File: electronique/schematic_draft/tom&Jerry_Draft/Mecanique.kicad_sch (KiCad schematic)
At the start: 4 parts

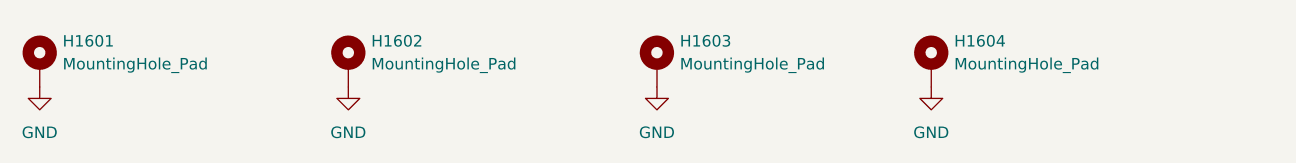
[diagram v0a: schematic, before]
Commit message: STM32 KiCAD v2.0 x CubeIDE - Pin definitif + schematic reviewed
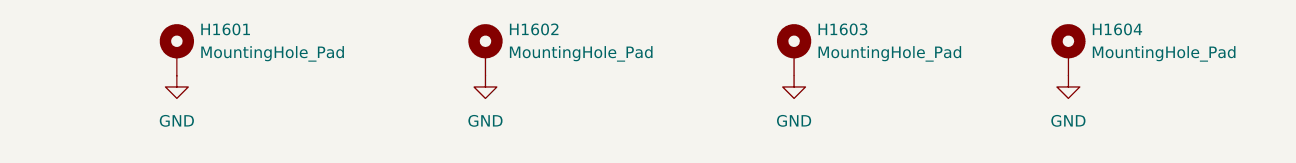
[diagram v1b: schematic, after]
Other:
- moved on the sheet: H1601, H1602, H1603, H1604
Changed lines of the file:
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@@
 	(symbol
 		(lib_id "power:GND")
-		(at 66.04 85.09 0)
+		(at 81.28 83.82 0)
 		(unit 1)
 		(exclude_from_sim no)
@@
 		(fields_autoplaced yes)
 		(property "Reference" "#PWR01601"
-			(at 66.04 91.44 0)
+			(at 81.28 90.17 0)
 			(effects
 				(font
@@
 		)
 		(property "Value" "GND"
-			(at 66.04 90.17 0)
-			(effects
-				(font
-					(size 1.27 1.27)
-				)
-			)
-		)
-		(property "Footprint" ""
-			(at 66.04 85.09 0)
+			(at 81.28 88.9 0)
+			(effects
+				(font
+					(size 1.27 1.27)
+				)
+			)
+		)
+		(property "Footprint" ""
+			(at 81.28 83.82 0)
 			(effects
 				(font
@@
 		)
 		(property "Datasheet" ""
-			(at 66.04 85.09 0)
+			(at 81.28 83.82 0)
 			(effects
 				(font
@@
 		)
 		(property "Description" "Power symbol creates a global label with name \"GND\" , ground"
-			(at 66.04 85.09 0)
+			(at 81.28 83.82 0)
 			(effects
 				(font
@@
 	(symbol
 		(lib_id "power:GND")
-		(at 165.1 85.09 0)
+		(at 180.34 83.82 0)
 		(unit 1)
 		(exclude_from_sim no)
@@
 		(fields_autoplaced yes)
 		(property "Reference" "#PWR01604"
-			(at 165.1 91.44 0)
+			(at 180.34 90.17 0)
 			(effects
 				(font
@@
 		)
 		(property "Value" "GND"
-			(at 165.1 90.17 0)
-			(effects
-				(font
-					(size 1.27 1.27)
-				)
-			)
-		)
-		(property "Footprint" ""
-			(at 165.1 85.09 0)
+			(at 180.34 88.9 0)
+			(effects
+				(font
+					(size 1.27 1.27)
+				)
+			)
+		)
+		(property "Footprint" ""
+			(at 180.34 83.82 0)
 			(effects
 				(font
@@
 		)
 		(property "Datasheet" ""
-			(at 165.1 85.09 0)
+			(at 180.34 83.82 0)
 			(effects
 				(font
@@
 		)
 		(property "Description" "Power symbol creates a global label with name \"GND\" , ground"
-			(at 165.1 85.09 0)
+			(at 180.34 83.82 0)
 			(effects
 				(font
@@
 	(symbol
 		(lib_id "Mechanical:MountingHole_Pad")
-		(at 134.62 82.55 0)
+		(at 149.86 81.28 0)
 		(unit 1)
 		(exclude_from_sim yes)
@@
 		(fields_autoplaced yes)
 		(property "Reference" "H1603"
-			(at 137.16 80.0099 0)
+			(at 152.4 78.7399 0)
 			(effects
 				(font
@@
 		)
 		(property "Value" "MountingHole_Pad"
-			(at 137.16 82.5499 0)
-			(effects
-				(font
-					(size 1.27 1.27)
-				)
-				(justify left)
-			)
-		)
-		(property "Footprint" ""
-			(at 134.62 82.55 0)
+			(at 152.4 81.2799 0)
+			(effects
+				(font
+					(size 1.27 1.27)
+				)
+				(justify left)
+			)
+		)
+		(property "Footprint" ""
+			(at 149.86 81.28 0)
 			(effects
 				(font
@@
 		)
 		(property "Datasheet" "~"
-			(at 134.62 82.55 0)
+			(at 149.86 81.28 0)
 			(effects
 				(font
@@
 		)
 		(property "Description" "Mounting Hole with connection"
-			(at 134.62 82.55 0)
+			(at 149.86 81.28 0)
 			(effects
 				(font
@@
 	(symbol
 		(lib_id "power:GND")
-		(at 100.33 85.09 0)
+		(at 115.57 83.82 0)
 		(unit 1)
 		(exclude_from_sim no)
@@
 		(fields_autoplaced yes)
 		(property "Reference" "#PWR01602"
-			(at 100.33 91.44 0)
+			(at 115.57 90.17 0)
 			(effects
 				(font
@@
 		)
 		(property "Value" "GND"
-			(at 100.33 90.17 0)
-			(effects
-				(font
-					(size 1.27 1.27)
-				)
-			)
-		)
-		(property "Footprint" ""
-			(at 100.33 85.09 0)
+			(at 115.57 88.9 0)
+			(effects
+				(font
+					(size 1.27 1.27)
+				)
+			)
+		)
+		(property "Footprint" ""
+			(at 115.57 83.82 0)
 			(effects
 				(font
@@
 		)
 		(property "Datasheet" ""
-			(at 100.33 85.09 0)
+			(at 115.57 83.82 0)
 			(effects
 				(font
@@
 		)
 		(property "Description" "Power symbol creates a global label with name \"GND\" , ground"
-			(at 100.33 85.09 0)
+			(at 115.57 83.82 0)
 			(effects
 				(font
@@
 	(symbol
 		(lib_id "power:GND")
-		(at 134.62 85.09 0)
+		(at 149.86 83.82 0)
 		(unit 1)
 		(exclude_from_sim no)
@@
 		(fields_autoplaced yes)
 		(property "Reference" "#PWR01603"
-			(at 134.62 91.44 0)
+			(at 149.86 90.17 0)
 			(effects
 				(font
@@
 		)
 		(property "Value" "GND"
-			(at 134.62 90.17 0)
-			(effects
-				(font
-					(size 1.27 1.27)
-				)
-			)
-		)
-		(property "Footprint" ""
-			(at 134.62 85.09 0)
+			(at 149.86 88.9 0)
+			(effects
+				(font
+					(size 1.27 1.27)
+				)
+			)
+		)
+		(property "Footprint" ""
+			(at 149.86 83.82 0)
 			(effects
 				(font
@@
 		)
 		(property "Datasheet" ""
-			(at 134.62 85.09 0)
+			(at 149.86 83.82 0)
 			(effects
 				(font
@@
 		)
 		(property "Description" "Power symbol creates a global label with name \"GND\" , ground"
-			(at 134.62 85.09 0)
+			(at 149.86 83.82 0)
 			(effects
 				(font
@@
 	(symbol
 		(lib_id "Mechanical:MountingHole_Pad")
-		(at 66.04 82.55 0)
+		(at 81.28 81.28 0)
 		(unit 1)
 		(exclude_from_sim yes)
@@
 		(fields_autoplaced yes)
 		(property "Reference" "H1601"
-			(at 68.58 80.0099 0)
+			(at 83.82 78.7399 0)
 			(effects
 				(font
@@
 		)
 		(property "Value" "MountingHole_Pad"
-			(at 68.58 82.5499 0)
-			(effects
-				(font
-					(size 1.27 1.27)
-				)
-				(justify left)
-			)
-		)
-		(property "Footprint" ""
-			(at 66.04 82.55 0)
+			(at 83.82 81.2799 0)
+			(effects
+				(font
+					(size 1.27 1.27)
+				)
+				(justify left)
+			)
+		)
+		(property "Footprint" ""
+			(at 81.28 81.28 0)
 			(effects
 				(font
@@
 		)
 		(property "Datasheet" "~"
-			(at 66.04 82.55 0)
+			(at 81.28 81.28 0)
 			(effects
 				(font
@@
 		)
 		(property "Description" "Mounting Hole with connection"
-			(at 66.04 82.55 0)
+			(at 81.28 81.28 0)
 			(effects
 				(font
@@
 	(symbol
 		(lib_id "Mechanical:MountingHole_Pad")
-		(at 165.1 82.55 0)
+		(at 180.34 81.28 0)
 		(unit 1)
 		(exclude_from_sim yes)
@@
 		(fields_autoplaced yes)
 		(property "Reference" "H1604"
-			(at 167.64 80.0099 0)
+			(at 182.88 78.7399 0)
 			(effects
 				(font
@@
 		)
 		(property "Value" "MountingHole_Pad"
-			(at 167.64 82.5499 0)
-			(effects
-				(font
-					(size 1.27 1.27)
-				)
-				(justify left)
-			)
-		)
-		(property "Footprint" ""
-			(at 165.1 82.55 0)
+			(at 182.88 81.2799 0)
+			(effects
+				(font
+					(size 1.27 1.27)
+				)
+				(justify left)
+			)
+		)
+		(property "Footprint" ""
+			(at 180.34 81.28 0)
 			(effects
 				(font
@@
 		)
 		(property "Datasheet" "~"
-			(at 165.1 82.55 0)
+			(at 180.34 81.28 0)
 			(effects
 				(font
@@
 		)
 		(property "Description" "Mounting Hole with connection"
-			(at 165.1 82.55 0)
+			(at 180.34 81.28 0)
 			(effects
 				(font
@@
 	(symbol
 		(lib_id "Mechanical:MountingHole_Pad")
-		(at 100.33 82.55 0)
+		(at 115.57 81.28 0)
 		(unit 1)
 		(exclude_from_sim yes)
@@
 		(fields_autoplaced yes)
 		(property "Reference" "H1602"
-			(at 102.87 80.0099 0)
+			(at 118.11 78.7399 0)
 			(effects
 				(font
@@
 		)
 		(property "Value" "MountingHole_Pad"
-			(at 102.87 82.5499 0)
-			(effects
-				(font
-					(size 1.27 1.27)
-				)
-				(justify left)
-			)
-		)
-		(property "Footprint" ""
-			(at 100.33 82.55 0)
+			(at 118.11 81.2799 0)
+			(effects
+				(font
+					(size 1.27 1.27)
+				)
+				(justify left)
+			)
+		)
+		(property "Footprint" ""
+			(at 115.57 81.28 0)
 			(effects
 				(font
@@
 		)
 		(property "Datasheet" "~"
-			(at 100.33 82.55 0)
+			(at 115.57 81.28 0)
 			(effects
 				(font
@@
 		)
 		(property "Description" "Mounting Hole with connection"
-			(at 100.33 82.55 0)
-			(effects
-				(font
+			(at 115.57 81.28 0)
+			(effects
+				(font

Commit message: Adding footprint V0.1
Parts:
- H1601, H1602, H1603, H1604: footprint (none) -> MountingHole:MountingHole_3.2mm_M3_Pad_Via
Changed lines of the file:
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@@
 			)
 		)
-		(property "Footprint" ""
+		(property "Footprint" "MountingHole:MountingHole_3.2mm_M3_Pad_Via"
 			(at 149.86 81.28 0)
 			(effects
@@
 			)
 		)
-		(property "Footprint" ""
+		(property "Footprint" "MountingHole:MountingHole_3.2mm_M3_Pad_Via"
 			(at 81.28 81.28 0)
 			(effects
@@
 			)
 		)
-		(property "Footprint" ""
+		(property "Footprint" "MountingHole:MountingHole_3.2mm_M3_Pad_Via"
 			(at 180.34 81.28 0)
 			(effects
@@
 			)
 		)
-		(property "Footprint" ""
+		(property "Footprint" "MountingHole:MountingHole_3.2mm_M3_Pad_Via"
 			(at 115.57 81.28 0)
 			(effects

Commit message: Ajout V2 TOF + MultiPCB Panalize
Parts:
- renumbered H1601 to H1101, H1602 to H1102, H1603 to H1103, H1604 to H1104
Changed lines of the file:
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@@
 		(dnp no)
 		(fields_autoplaced yes)
-		(property "Reference" "#PWR01601"
+		(property "Reference" "#PWR01101"
 			(at 81.28 90.17 0)
 			(effects
@@
 			(project ""
 				(path "/d6e3fbeb-d028-494d-83bf-2e4a8b12578d/ea2dc0aa-c072-4ac8-b7d3-16b9d53a67a9"
-					(reference "#PWR01601")
+					(reference "#PWR01101")
 					(unit 1)
 				)
@@
 		(dnp no)
 		(fields_autoplaced yes)
-		(property "Reference" "#PWR01604"
+		(property "Reference" "#PWR01104"
 			(at 180.34 90.17 0)
 			(effects
@@
 			(project "tom&Jerry_Draft"
 				(path "/d6e3fbeb-d028-494d-83bf-2e4a8b12578d/ea2dc0aa-c072-4ac8-b7d3-16b9d53a67a9"
-					(reference "#PWR01604")
+					(reference "#PWR01104")
 					(unit 1)
 				)
@@
 		(dnp no)
 		(fields_autoplaced yes)
-		(property "Reference" "H1603"
+		(property "Reference" "H1103"
 			(at 152.4 78.7399 0)
 			(effects
@@
 			(project "tom&Jerry_Draft"
 				(path "/d6e3fbeb-d028-494d-83bf-2e4a8b12578d/ea2dc0aa-c072-4ac8-b7d3-16b9d53a67a9"
-					(reference "H1603")
+					(reference "H1103")
 					(unit 1)
 				)
@@
 		(dnp no)
 		(fields_autoplaced yes)
-		(property "Reference" "#PWR01602"
+		(property "Reference" "#PWR01102"
 			(at 115.57 90.17 0)
 			(effects
@@
 			(project "tom&Jerry_Draft"
 				(path "/d6e3fbeb-d028-494d-83bf-2e4a8b12578d/ea2dc0aa-c072-4ac8-b7d3-16b9d53a67a9"
-					(reference "#PWR01602")
+					(reference "#PWR01102")
 					(unit 1)
 				)
@@
 		(dnp no)
 		(fields_autoplaced yes)
-		(property "Reference" "#PWR01603"
+		(property "Reference" "#PWR01103"
 			(at 149.86 90.17 0)
 			(effects
@@
 			(project "tom&Jerry_Draft"
 				(path "/d6e3fbeb-d028-494d-83bf-2e4a8b12578d/ea2dc0aa-c072-4ac8-b7d3-16b9d53a67a9"
-					(reference "#PWR01603")
+					(reference "#PWR01103")
 					(unit 1)
 				)
@@
 		(dnp no)
 		(fields_autoplaced yes)
-		(property "Reference" "H1601"
+		(property "Reference" "H1101"
 			(at 83.82 78.7399 0)
 			(effects
@@
 			(project ""
 				(path "/d6e3fbeb-d028-494d-83bf-2e4a8b12578d/ea2dc0aa-c072-4ac8-b7d3-16b9d53a67a9"
-					(reference "H1601")
+					(reference "H1101")
 					(unit 1)
 				)
@@
 		(dnp no)
 		(fields_autoplaced yes)
-		(property "Reference" "H1604"
+		(property "Reference" "H1104"
 			(at 182.88 78.7399 0)
 			(effects
@@
 			(project "tom&Jerry_Draft"
 				(path "/d6e3fbeb-d028-494d-83bf-2e4a8b12578d/ea2dc0aa-c072-4ac8-b7d3-16b9d53a67a9"
-					(reference "H1604")
+					(reference "H1104")
 					(unit 1)
 				)
@@
 		(dnp no)
 		(fields_autoplaced yes)
-		(property "Reference" "H1602"
+		(property "Reference" "H1102"
 			(at 118.11 78.7399 0)
 			(effects
@@
 			(project "tom&Jerry_Draft"
 				(path "/d6e3fbeb-d028-494d-83bf-2e4a8b12578d/ea2dc0aa-c072-4ac8-b7d3-16b9d53a67a9"
-					(reference "H1602")
-					(unit 1)
-				)
+					(reference "H1102")
+					(unit 1)
+				)

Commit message: Routage Signal Complet - PCB V2.0
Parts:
- renumbered H1101 to H1201, H1102 to H1202, H1103 to H1203, H1104 to H1204
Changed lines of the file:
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@@
 		(dnp no)
 		(fields_autoplaced yes)
-		(property "Reference" "#PWR01101"
+		(property "Reference" "#PWR01201"
 			(at 81.28 90.17 0)
 			(effects
@@
 			(project ""
 				(path "/d6e3fbeb-d028-494d-83bf-2e4a8b12578d/ea2dc0aa-c072-4ac8-b7d3-16b9d53a67a9"
-					(reference "#PWR01101")
+					(reference "#PWR01201")
 					(unit 1)
 				)
@@
 		(dnp no)
 		(fields_autoplaced yes)
-		(property "Reference" "#PWR01104"
+		(property "Reference" "#PWR01204"
 			(at 180.34 90.17 0)
 			(effects
@@
 			(project "tom&Jerry_Draft"
 				(path "/d6e3fbeb-d028-494d-83bf-2e4a8b12578d/ea2dc0aa-c072-4ac8-b7d3-16b9d53a67a9"
-					(reference "#PWR01104")
+					(reference "#PWR01204")
 					(unit 1)
 				)
@@
 		(dnp no)
 		(fields_autoplaced yes)
-		(property "Reference" "H1103"
+		(property "Reference" "H1203"
 			(at 152.4 78.7399 0)
 			(effects
@@
 			(project "tom&Jerry_Draft"
 				(path "/d6e3fbeb-d028-494d-83bf-2e4a8b12578d/ea2dc0aa-c072-4ac8-b7d3-16b9d53a67a9"
-					(reference "H1103")
+					(reference "H1203")
 					(unit 1)
 				)
@@
 		(dnp no)
 		(fields_autoplaced yes)
-		(property "Reference" "#PWR01102"
+		(property "Reference" "#PWR01202"
 			(at 115.57 90.17 0)
 			(effects
@@
 			(project "tom&Jerry_Draft"
 				(path "/d6e3fbeb-d028-494d-83bf-2e4a8b12578d/ea2dc0aa-c072-4ac8-b7d3-16b9d53a67a9"
-					(reference "#PWR01102")
+					(reference "#PWR01202")
 					(unit 1)
 				)
@@
 		(dnp no)
 		(fields_autoplaced yes)
-		(property "Reference" "#PWR01103"
+		(property "Reference" "#PWR01203"
 			(at 149.86 90.17 0)
 			(effects
@@
 			(project "tom&Jerry_Draft"
 				(path "/d6e3fbeb-d028-494d-83bf-2e4a8b12578d/ea2dc0aa-c072-4ac8-b7d3-16b9d53a67a9"
-					(reference "#PWR01103")
+					(reference "#PWR01203")
 					(unit 1)
 				)
@@
 		(dnp no)
 		(fields_autoplaced yes)
-		(property "Reference" "H1101"
+		(property "Reference" "H1201"
 			(at 83.82 78.7399 0)
 			(effects
@@
 			(project ""
 				(path "/d6e3fbeb-d028-494d-83bf-2e4a8b12578d/ea2dc0aa-c072-4ac8-b7d3-16b9d53a67a9"
-					(reference "H1101")
+					(reference "H1201")
 					(unit 1)
 				)
@@
 		(dnp no)
 		(fields_autoplaced yes)
-		(property "Reference" "H1104"
+		(property "Reference" "H1204"
 			(at 182.88 78.7399 0)
 			(effects
@@
 			(project "tom&Jerry_Draft"
 				(path "/d6e3fbeb-d028-494d-83bf-2e4a8b12578d/ea2dc0aa-c072-4ac8-b7d3-16b9d53a67a9"
-					(reference "H1104")
+					(reference "H1204")
 					(unit 1)
 				)
@@
 		(dnp no)
 		(fields_autoplaced yes)
-		(property "Reference" "H1102"
+		(property "Reference" "H1202"
 			(at 118.11 78.7399 0)
 			(effects
@@
 			(project "tom&Jerry_Draft"
 				(path "/d6e3fbeb-d028-494d-83bf-2e4a8b12578d/ea2dc0aa-c072-4ac8-b7d3-16b9d53a67a9"
-					(reference "H1102")
-					(unit 1)
-				)
+					(reference "H1202")
+					(unit 1)
+				)
